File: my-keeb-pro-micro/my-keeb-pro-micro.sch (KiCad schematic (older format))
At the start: 108 parts, among them SW1 SW_Push, U1 ATmega32U4-AU, Y1 16MHz

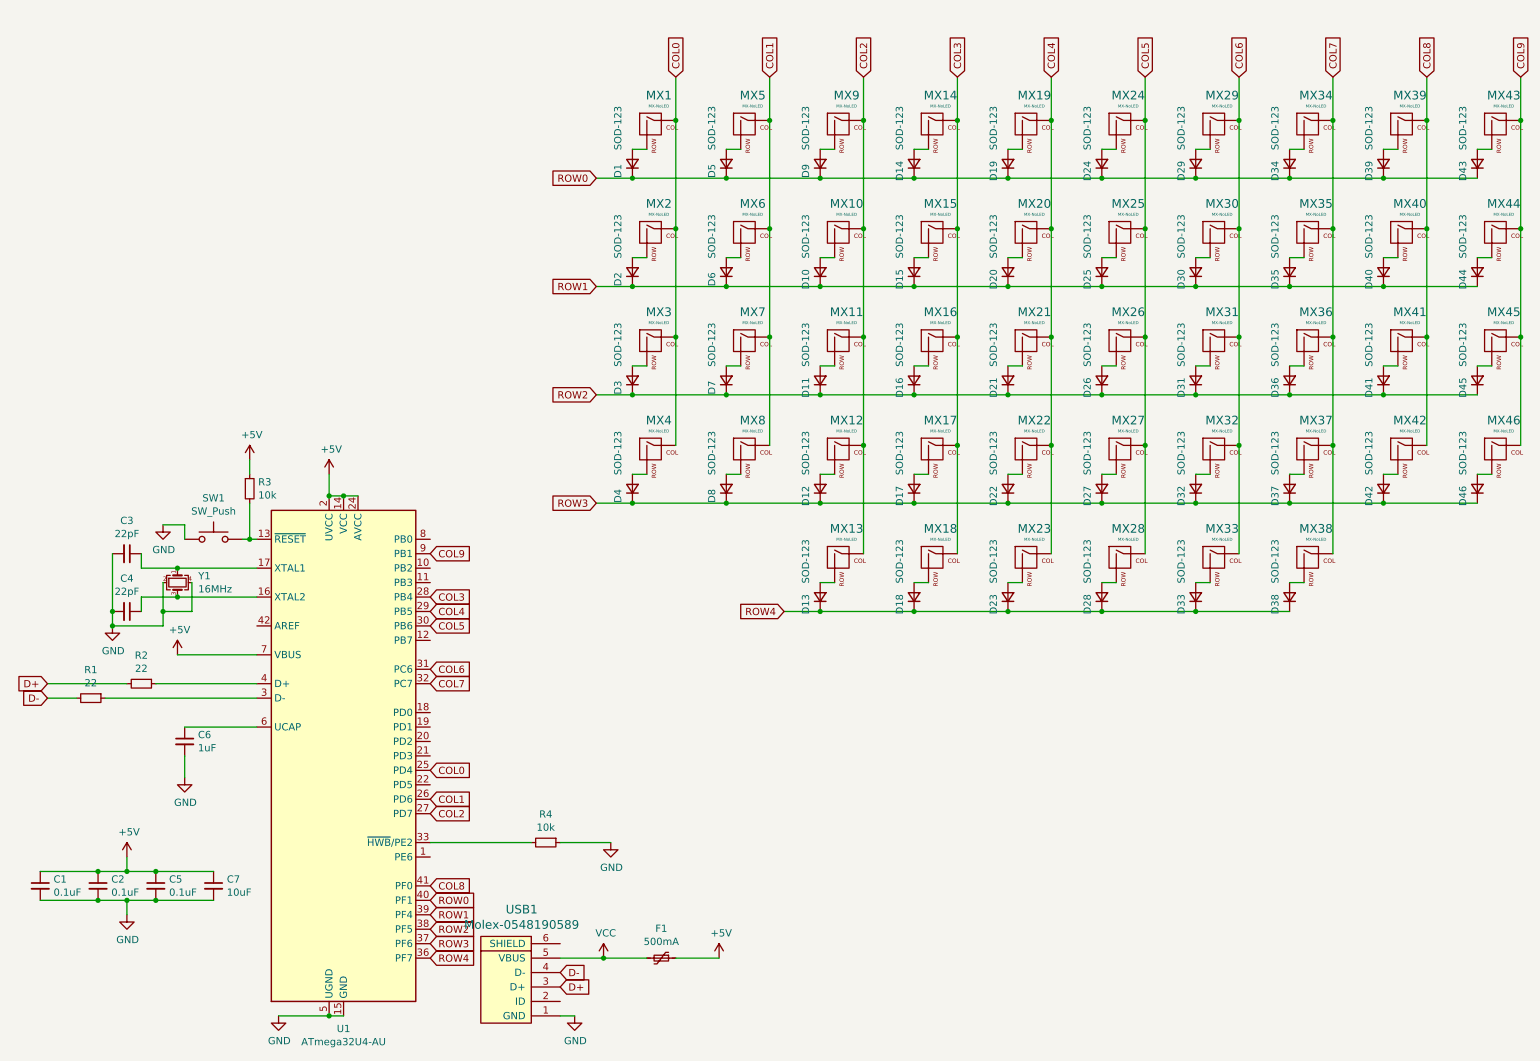
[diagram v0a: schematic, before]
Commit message: Updated my-keeb pcb
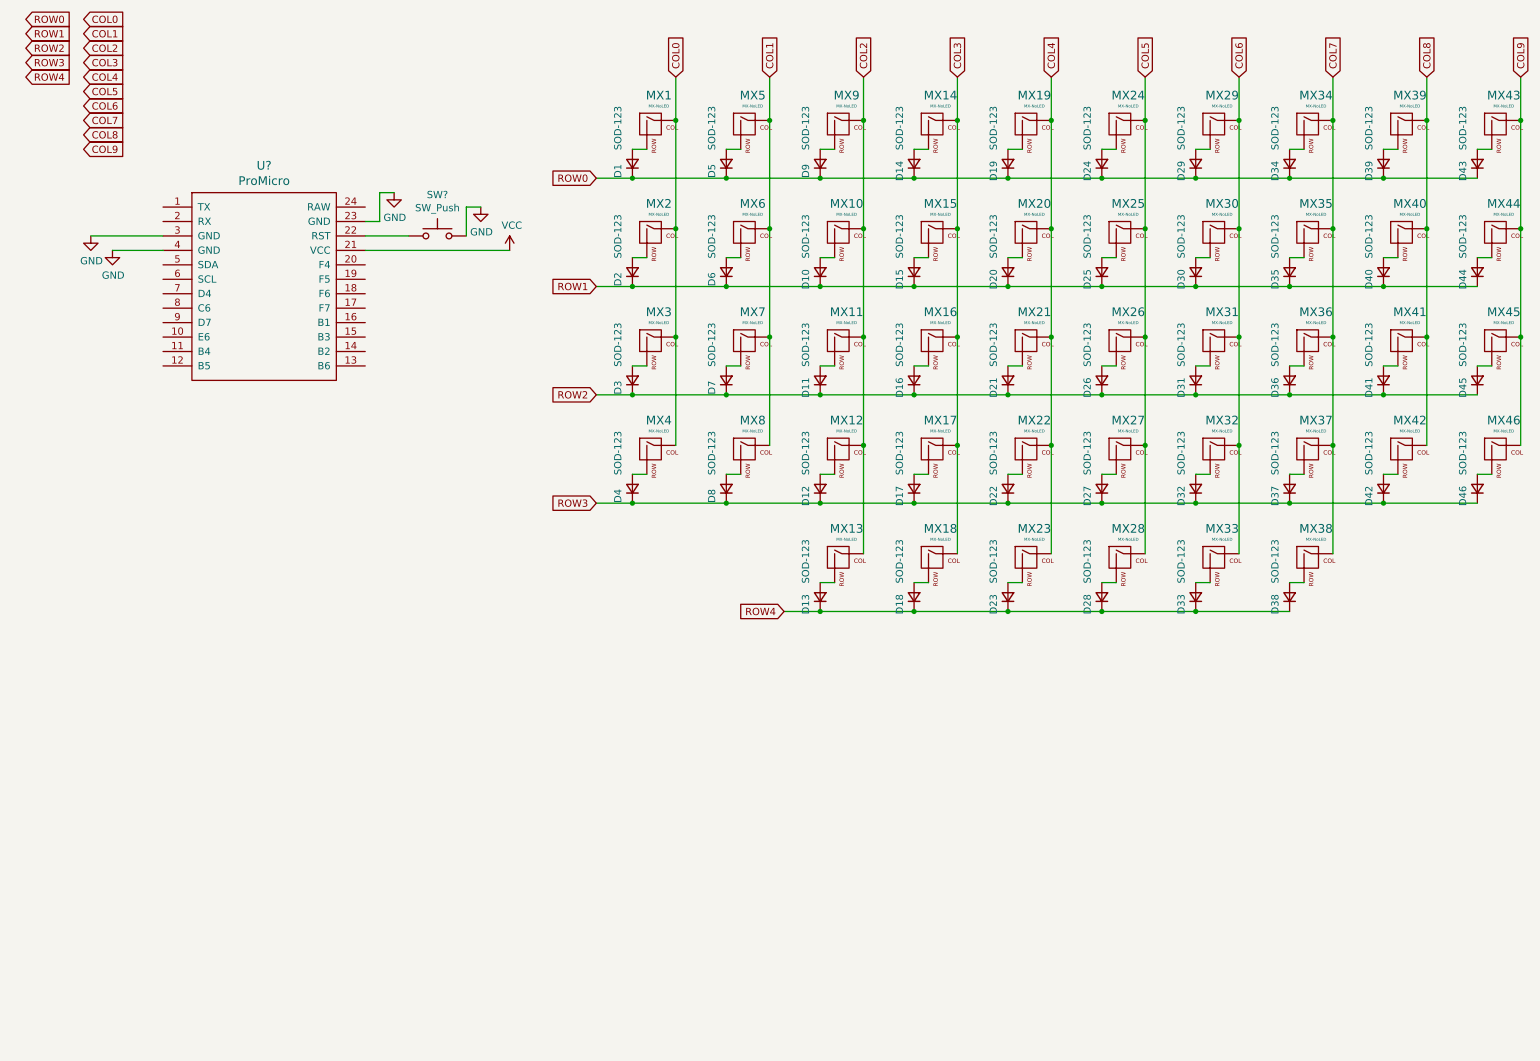
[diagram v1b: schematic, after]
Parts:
- removed C1, C2, C5: 0.1uF, Capacitor_SMD:C_0805_2012Metric, symbol Device:C_Small
- removed C3, C4: 22pF, Capacitor_SMD:C_0805_2012Metric, symbol Device:C_Small
- removed C6: 1uF, Capacitor_SMD:C_0805_2012Metric, symbol Device:C_Small
- removed C7: 10uF, Capacitor_SMD:C_0805_2012Metric, symbol Device:C_Small
- removed F1: 500mA, Fuse:Fuse_1206_3216Metric, symbol Device:Polyfuse_Small
- removed R1, R2: 22, Resistor_SMD:R_0805_2012Metric, symbol Device:R_Small
- removed R3, R4: 10k, Resistor_SMD:R_0805_2012Metric, symbol Device:R_Small
- removed SW1: SW_Push, random-keyboard-parts:SKQG-1155865, symbol Switch:SW_Push
- removed U1: ATmega32U4-AU, Package_QFP:TQFP-44_10x10mm_P0.8mm, symbol MCU_Microchip_ATmega:ATmega32U4-AU
- removed USB1: Molex-0548190589, random-keyboard-parts:Molex-0548190589, symbol random-keyboard-parts:Molex-0548190589
- removed Y1: 16MHz, Crystal:Crystal_SMD_3225-4Pin_3.2x2.5mm, symbol Device:Crystal_GND24_Small
- added SW?: SW_Push, symbol Switch:SW_Push
- added U?: ProMicro, symbol promicro:ProMicro
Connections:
- net GND: now also SW?.2, U?.23 (GND), U?.3 (GND), U?.4 (GND)
- net VCC: now also U?.21 (VCC)
- new net: SW?.1, U?.22 (RST)

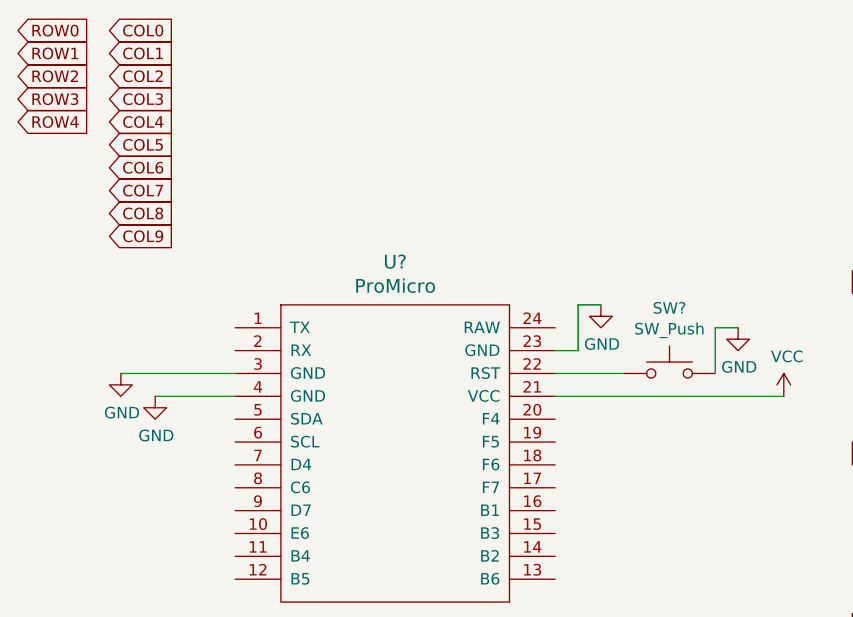
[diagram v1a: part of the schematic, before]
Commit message: Added pro micro to pcb, routing WIP
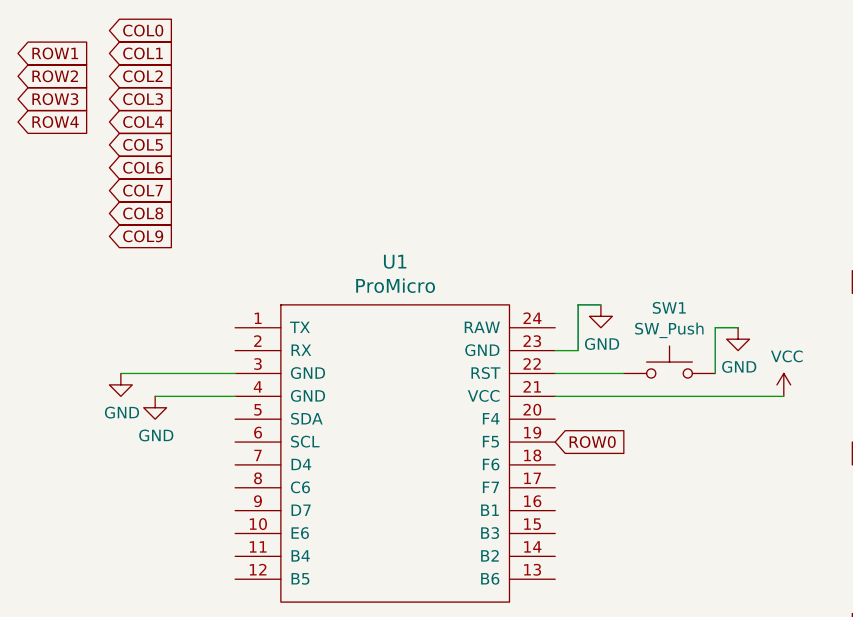
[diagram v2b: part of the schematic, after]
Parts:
- SW1: renamed from SW?; footprint (none) -> random-keyboard-parts:SKQG-1155865
- U1: renamed from U?; footprint (none) -> promicro:ProMicro
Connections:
- net ROW0: now also U1.19 (F5)
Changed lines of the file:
@@
 COL9
 $Comp
-L power:GND #PWR?
+L power:GND #PWR0101
 U 1 1 61D6CE67
 P 1150 2200
-F 0 "#PWR?" H 1150 1950 50  0001 C CNN
+F 0 "#PWR0101" H 1150 1950 50  0001 C CNN
 F 1 "GND" H 1155 2027 50  0000 C CNN
 F 2 "" H 1150 2200 50  0001 C CNN
@@
 $EndComp
 $Comp
-L power:GND #PWR?
+L power:GND #PWR0102
 U 1 1 61D6ECB5
 P 1000 2100
-F 0 "#PWR?" H 1000 1850 50  0001 C CNN
+F 0 "#PWR0102" H 1000 1850 50  0001 C CNN
 F 1 "GND" H 1005 1927 50  0000 C CNN
 F 2 "" H 1000 2100 50  0001 C CNN
@@
 	1500 2200 1150 2200
 $Comp
-L power:GND #PWR?
+L power:GND #PWR0103
 U 1 1 61D92BAD
 P 3100 1800
-F 0 "#PWR?" H 3100 1550 50  0001 C CNN
+F 0 "#PWR0103" H 3100 1550 50  0001 C CNN
 F 1 "GND" H 3105 1627 50  0000 C CNN
 F 2 "" H 3100 1800 50  0001 C CNN
@@
 	2900 2100 3200 2100
 $Comp
-L Switch:SW_Push SW?
+L Switch:SW_Push SW1
 U 1 1 61D27B43
 P 3400 2100
-F 0 "SW?" H 3400 2385 50  0000 C CNN
+F 0 "SW1" H 3400 2385 50  0000 C CNN
 F 1 "SW_Push" H 3400 2294 50  0000 C CNN
-F 2 "" H 3400 2300 50  0001 C CNN
+F 2 "random-keyboard-parts:SKQG-1155865" H 3400 2300 50  0001 C CNN
 F 3 "~" H 3400 2300 50  0001 C CNN
 	1    3400 2100
@@
 	3000 1800 3100 1800
 $Comp
-L power:VCC #PWR?
+L power:VCC #PWR0104
 U 1 1 61DD10AC
 P 3900 2200
-F 0 "#PWR?" H 3900 2050 50  0001 C CNN
+F 0 "#PWR0104" H 3900 2050 50  0001 C CNN
 F 1 "VCC" H 3915 2373 50  0000 C CNN
 F 2 "" H 3900 2200 50  0001 C CNN
@@
 $EndComp
 $Comp
-L promicro:ProMicro U?
+L promicro:ProMicro U1
 U 1 1 61D06E1E
 P 2200 2650
-F 0 "U?" H 2200 3687 60  0000 C CNN
+F 0 "U1" H 2200 3687 60  0000 C CNN
 F 1 "ProMicro" H 2200 3581 60  0000 C CNN
-F 2 "" H 2300 1600 60  0000 C CNN
+F 2 "promicro:ProMicro" H 2300 1600 60  0001 C CNN
 F 3 "" H 2300 1600 60  0000 C CNN
 	1    2200 2650
@@
 	2900 2200 3900 2200
 $Comp
-L power:GND #PWR?
+L power:GND #PWR0105
 U 1 1 61DAFE42
 P 3700 1900
-F 0 "#PWR?" H 3700 1650 50  0001 C CNN
+F 0 "#PWR0105" H 3700 1650 50  0001 C CNN
 F 1 "GND" H 3705 1727 50  0000 C CNN
 F 2 "" H 3700 1900 50  0001 C CNN
@@
 Text GLabel 950  1400 2    50   Input ~ 0
 COL8
-Text GLabel 550  600  2    50   Input ~ 0
+Text GLabel 2900 2400 2    50   Input ~ 0
 ROW0
 Text GLabel 550  700  2    50   Input ~ 0

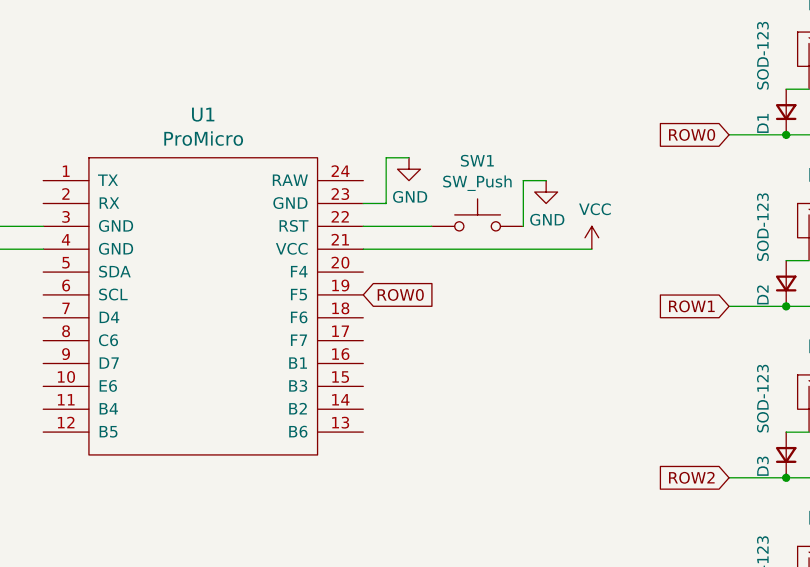
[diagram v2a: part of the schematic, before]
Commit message: Added some footprints prettys
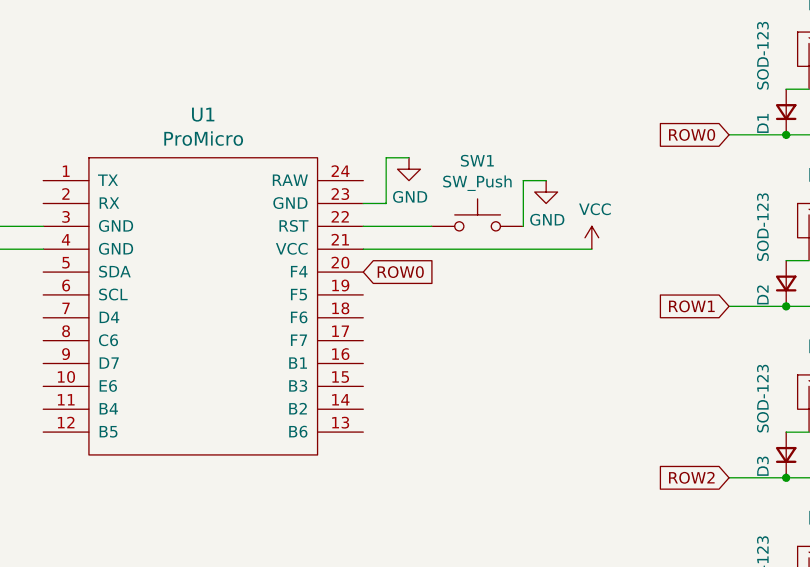
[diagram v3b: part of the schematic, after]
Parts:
- D1, D10, D11, D12, D13, D14, D15, D16, D17, D18, D19, D2, D20, D21, D22, D23, D24, D25, D26, D27, D28, D29, D3, D30, D31, D32, D33, D34, D35, D36, D37, D38, D39, D4, D40, D41, D42, D43, D44, D45, D46, D5, D6, D7, D8, D9: footprint Diode_SMD:D_SOD-123 -> random-keyboard-parts:D_SOD-123-Pretty
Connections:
- net ROW0: now also U1.20 (F4); no longer U1.19 (F5)

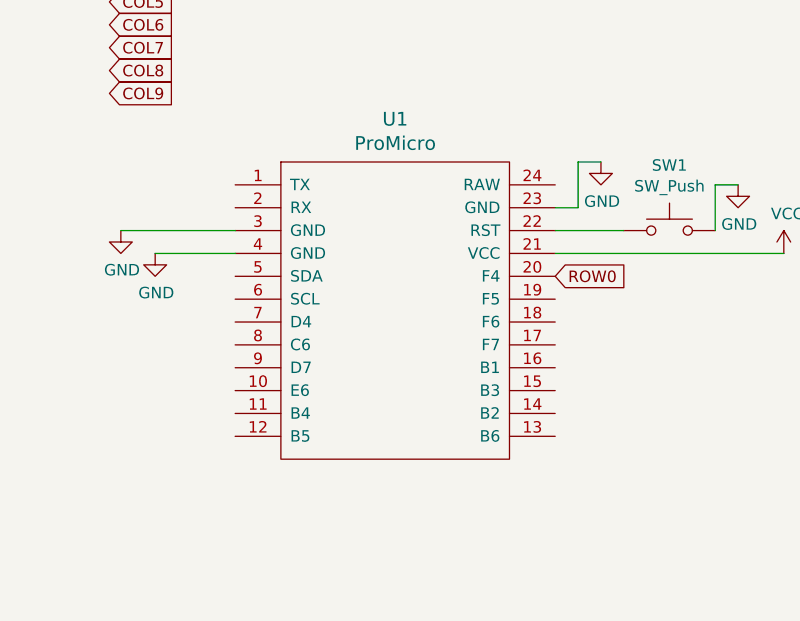
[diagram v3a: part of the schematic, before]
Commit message: Promicro pcb uses hybrid diodes
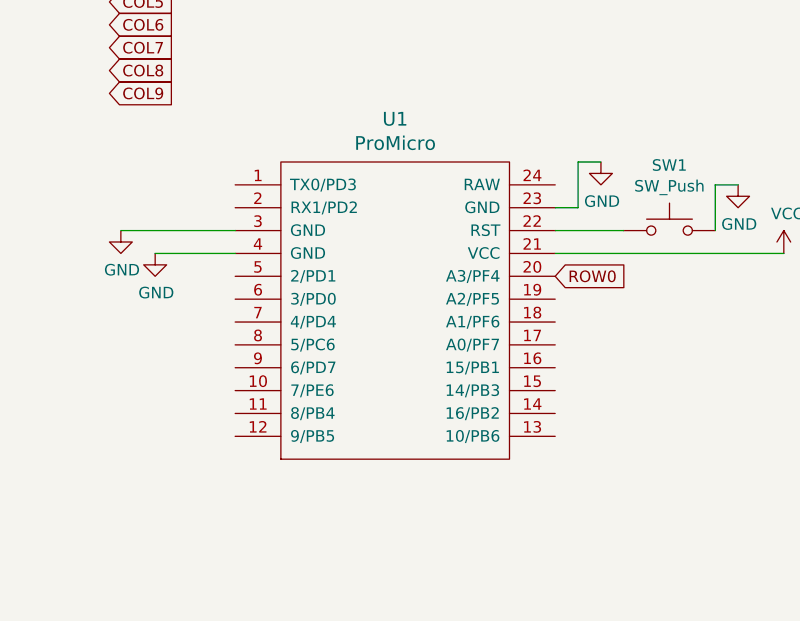
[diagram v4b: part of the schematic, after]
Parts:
- removed U1: ProMicro, promicro:ProMicro, symbol promicro:ProMicro
- added U1: ProMicro, Keebio-Parts:ArduinoProMicro-ZigZag, symbol keebio:ProMicro
- D1, D10, D11, D12, D13, D14, D15, D16, D17, D18, D19, D2, D20, D21, D22, D23, D24, D25, D26, D27, D28, D29, D3, D30, D31, D32, D33, D34, D35, D36, D37, D38, D39, D4, D40, D41, D42, D43, D44, D45, D46, D5, D6, D7, D8, D9: footprint random-keyboard-parts:D_SOD-123-Pretty -> Keebio-Parts:Diode-Hybrid-Back
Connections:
- net GND: now also U1.23 (GND), U1.3 (GND), U1.4 (GND)
- net ROW0: now also U1.20 (A3/PF4)
- net VCC: now also U1.21 (VCC)
- net at SW1.1: now also U1.22 (RST)

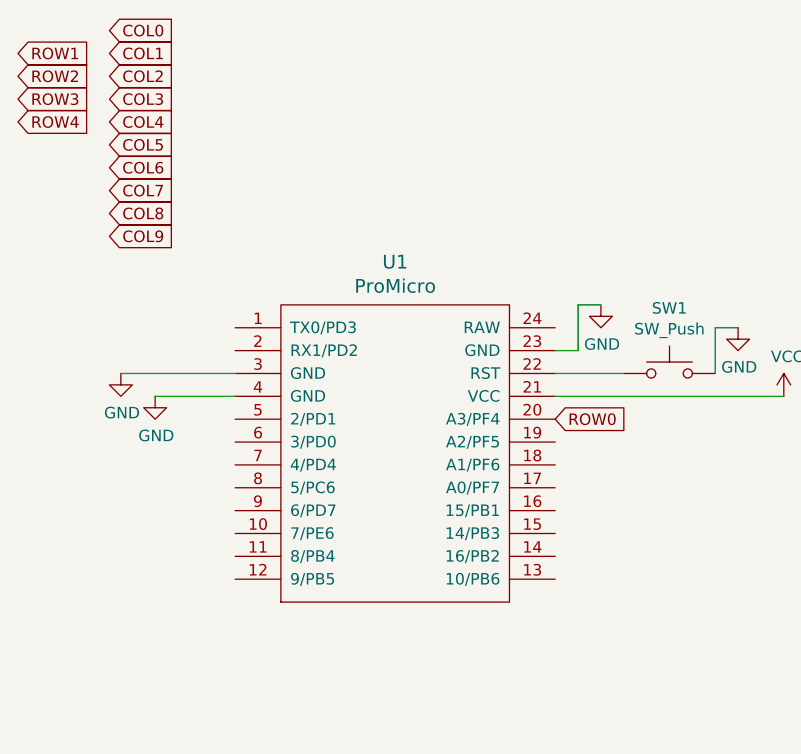
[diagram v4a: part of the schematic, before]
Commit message: Finished pro micro pcb
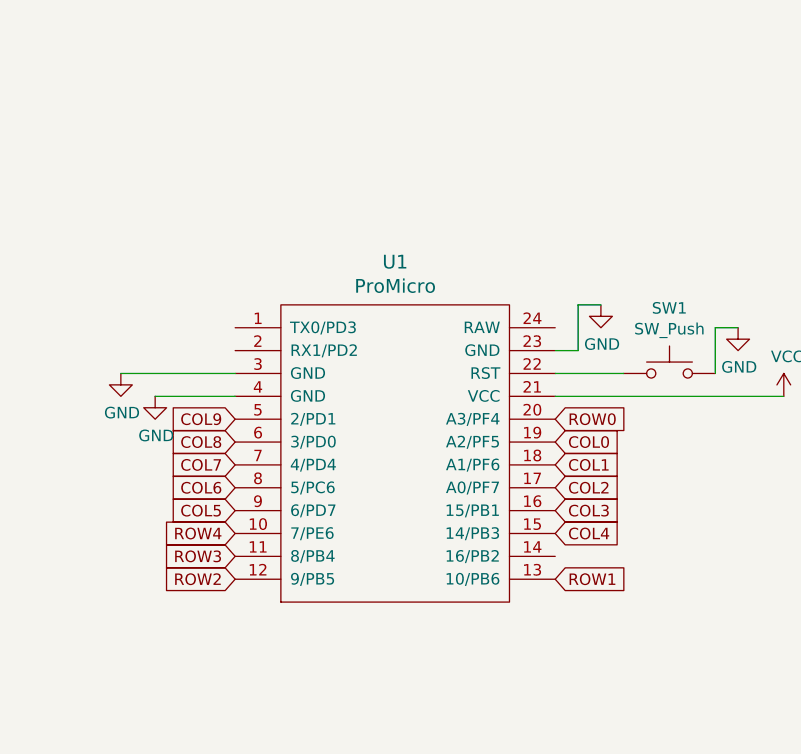
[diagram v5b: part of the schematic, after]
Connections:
- net COL0: now also U1.19 (A2/PF5)
- net COL1: now also U1.18 (A1/PF6)
- net COL2: now also U1.17 (A0/PF7)
- net COL3: now also U1.16 (15/PB1)
- net COL4: now also U1.15 (14/PB3)
- net COL5: now also U1.9 (6/PD7)
- net COL6: now also U1.8 (5/PC6)
- net COL7: now also U1.7 (4/PD4)
- net COL8: now also U1.6 (3/PD0)
- net COL9: now also U1.5 (2/PD1)
- net ROW1: now also U1.13 (10/PB6)
- net ROW2: now also U1.12 (9/PB5)
- net ROW3: now also U1.11 (8/PB4)
- net ROW4: now also U1.10 (7/PE6)
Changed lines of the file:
@@
 Text GLabel 10900 1000 1    50   Input ~ 0
 COL9
-Text GLabel 950  1500 2    50   Input ~ 0
+Text GLabel 1500 2300 0    50   Input ~ 0
 COL9
 $Comp
@@
 Wire Wire Line
 	3600 1900 3600 2100
-Text GLabel 950  1400 2    50   Input ~ 0
+Text GLabel 1500 2400 0    50   Input ~ 0
 COL8
 Text GLabel 2900 2300 2    50   Input ~ 0
 ROW0
-Text GLabel 550  700  2    50   Input ~ 0
+Text GLabel 2900 3000 2    50   Input ~ 0
 ROW1
-Text GLabel 550  800  2    50   Input ~ 0
+Text GLabel 1500 3000 0    50   Input ~ 0
 ROW2
-Text GLabel 550  900  2    50   Input ~ 0
+Text GLabel 1500 2900 0    50   Input ~ 0
 ROW3
-Text GLabel 950  600  2    50   Input ~ 0
+Text GLabel 2900 2400 2    50   Input ~ 0
 COL0
-Text GLabel 950  700  2    50   Input ~ 0
+Text GLabel 2900 2500 2    50   Input ~ 0
 COL1
-Text GLabel 950  800  2    50   Input ~ 0
+Text GLabel 2900 2600 2    50   Input ~ 0
 COL2
-Text GLabel 950  900  2    50   Input ~ 0
+Text GLabel 2900 2700 2    50   Input ~ 0
 COL3
-Text GLabel 950  1000 2    50   Input ~ 0
+Text GLabel 2900 2800 2    50   Input ~ 0
 COL4
-Text GLabel 950  1100 2    50   Input ~ 0
+Text GLabel 1500 2700 0    50   Input ~ 0
 COL5
-Text GLabel 950  1200 2    50   Input ~ 0
+Text GLabel 1500 2600 0    50   Input ~ 0
 COL6
-Text GLabel 950  1300 2    50   Input ~ 0
+Text GLabel 1500 2500 0    50   Input ~ 0
 COL7
-Text GLabel 550  1000 2    50   Input ~ 0
+Text GLabel 1500 2800 0    50   Input ~ 0
 ROW4
 Text GLabel 5800 4700 0    50   Input ~ 0
